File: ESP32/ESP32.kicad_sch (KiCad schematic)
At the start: 0 parts

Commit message: ESP32
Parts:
- added C1: C_Small, symbol Device:C_Small
- added D1: D, symbol Device:D
- added U1: ESP32-S3, Package_DFN_QFN:QFN-56-1EP_7x7mm_P0.4mm_EP4x4mm, symbol MCU_Espressif:ESP32-S3
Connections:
- new net: U1.2 (VDD3P3), U1.3 (VDD3P3)
- new net: U1.55 (VDDA), U1.56 (VDDA)

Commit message: Upload ESP32
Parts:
- added C1, C4, C5: TBD, symbol Device:C_Small
- added C10, C13, C14, C15: 0.1uF, symbol Device:C_Small
- added C2: 1u, symbol Device:C_Small
- added C3: 10n, symbol Device:C_Small
- added L2, L4, L5: 24nH, symbol Device:L
- added R1: 10k(NC), symbol Device:R_US
- added R10, R13, R14, R15, R16: 0, symbol Device:R_US
- added R3: 499, symbol Device:R_US
- added Y1: Crystal, symbol Device:Crystal
- C21: renamed from C1; value C_Small -> 10u
- D1: value D -> ESD
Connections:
- net +3V3: now also C21.1, D1.1 (K), U1.20 (VDD3P3_RTC), U1.46 (VDD3P3_CPU), C10.1, C15.1, C2.1, C3.1, R1.2
- net GNDREF: now also C21.2, D1.2 (A), U1.57 (GND), C1.2, C10.2, C13.2, C14.1, C15.2, C2.2, C4.2, C5.2
- net GPIO5: now reaches U1.10 (GPIO5)
- net GPIO6: now reaches U1.11 (GPIO6)
- net GPIO7: now reaches U1.12 (GPIO7)
- net GPIO8: now reaches U1.13 (GPIO8)
- net GPIO9: now reaches U1.14 (GPIO9)
- net GPIO10: now reaches U1.15 (GPIO10)
- net GPIO11: now reaches U1.16 (GPIO11)
- net GPIO12: now reaches U1.17 (GPIO12)
- net GPIO13: now reaches U1.18 (GPIO13)
- net GPIO14: now reaches U1.19 (GPIO14)
- net GPIO17: now reaches U1.23 (GPIO17)
- net GPIO18: now reaches U1.24 (GPIO18)
- net GPIO19: now reaches U1.25 (GPIO19/USB_D-)
- net GPIO20: now reaches U1.26 (GPIO20/USB_D+)
- net GPIO21: now reaches U1.27 (GPIO21)
- net GPIO26: now reaches U1.28 (SPICS1)
- net VDD_SPI: now reaches U1.29 (VDD_SPI)
- net VDD_SPI: now also C13.1, C14.2
- net at U1.30 (SPIHD): now also R13.2
- net at U1.31 (SPIWP): now also R14.2
- net SPIS0: now reaches U1.32 (SPICS0)
- net at U1.33 (SPICLK): now also R10.2
- net at U1.34 (SPIQ): now also R15.2
- net at U1.35 (SPID): now also R16.2
- net GPIO48: now reaches U1.36 (SPICLK_N)
- net GPIO47: now reaches U1.37 (SPICLK_P)
- net GPIO33: now reaches U1.38 (GPIO33)
- net GPIO34: now reaches U1.39 (GPIO34)
- net CHIP_PU: now reaches U1.4 (CHIP_PU)
- net GPIO35: now reaches U1.40 (GPIO35)
- net GPIO36: now reaches U1.41 (GPIO36)
- net GPIO37: now reaches U1.42 (GPIO37)
- net GPIO38: now reaches U1.43 (GPIO38)
- net GPIO39: now reaches U1.44 (MTCK)
- net GPIO40: now reaches U1.45 (MTDO)
- net GPIO41: now reaches U1.47 (MTDI)
- net GPIO42: now reaches U1.48 (MTMS)
- net at U1.49 (U0TXD): now also R3.2
- net GPIO0: now reaches U1.5 (GPIO0)
- net U0RXD: now reaches U1.50 (U0RXD)
- net GPIO45: now reaches U1.51 (GPIO45)
- net GPIO45: now also R1.1
- net GPIO46: now reaches U1.52 (GPIO46)
- net 40MHz(10ppm): now reaches U1.53 (XTAL_N)
- net 40MHz(10ppm): now also C4.1, L4.1, Y1.2
- net at U1.54 (XTAL_P): now also L4.2
- net at U1.55 (VDDA), U1.56 (VDDA): now also C3.2
- net GPIO1: now reaches U1.6 (GPIO1)
- net GPIO2: now reaches U1.7 (GPIO2)
- net GPIO3: now reaches U1.8 (GPIO3)
- net GPIO4: now reaches U1.9 (GPIO4)
- new net: C1.1, Y1.1
- new net LNA_IN: L2.1
- new net SPICLK: R10.1
- new net SPID: R16.1
- new net SPIHD: R13.1
- new net SPIQ: R15.1
- new net SPIWP: R14.1
- new net U0TXD: R3.1
- no-connect marks 0 -> 1
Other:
- title: (none) -> ESP32-S3
- moved on the sheet: C21, D1, U1

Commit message: Upload ESP32
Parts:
- added U2: W25Q128JV, Package_SON:WSON-8-1EP_8x6mm_P1.27mm_EP3.4x4.3mm, symbol Memory_Flash:W25Q128JVE
- added U3: APS1604M-3SQRx-SN, Package_SO:SOIC-8_3.9x4.9mm_P1.27mm, symbol Memory_RAM:APS1604M-3SQRx-SN
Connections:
- net GNDREF: now also U2.4 (GND)
- net SPICLK: now also U2.6 (CLK)
- net SPID: now also U2.2 (DO/IO_{1})
- net SPIHD: now also U2.5 (DI/IO_{0})
- net SPIQ: now also U2.3 (~{WP}/IO_{2})
- net SPIWP: now also U2.7 (~{HOLD}/~{RESET}/IO_{3})
- new net SPICS0: U2.1 (~{CS})
- new net VDD: U2.8 (VCC)

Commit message: Upload ESP32
Version 5
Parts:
- added C6, C7: C_Small, symbol Device:C_Small
- added P1: USB_C_Plug_USB2.0, symbol Connector:USB_C_Plug_USB2.0
- added R13, R14: 22/33, symbol Device:R_US
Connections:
- net GNDREF: now also U3.4 (VSS), C6.1, C7.2
- net GPIO26: now also U3.1 (~{CE})
- net SPICLK: now also U3.6 (SCLK)
- net SPID: now also U3.5 (SI/SIO0)
- net SPIHD: now also U3.7 (SIO3)
- net SPIQ: now also U3.2 (SO/SIO1)
- net SPIWP: now also U3.3 (SIO2)
- net VDD: now also U3.8 (VDD)
- new net: C7.1, P1.A6 (D+), R14.1
- new net: P1.A1 (GND), P1.A12 (GND), P1.B1 (GND), P1.B12 (GND)
- new net: P1.A4 (VBUS), P1.A9 (VBUS), P1.B4 (VBUS), P1.B9 (VBUS)
- new net: C6.2, P1.A7 (D-), R13.1
- new net USB_DM: R14.2
- new net USB_DP: R13.2
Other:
- added sheet Wi-Fi Module (Wi-Fi Module_sch.kicad_sch)
- note added: "FLASH-3V3"
- note added: "PSRAM-3V3"
- moved on the sheet: U3

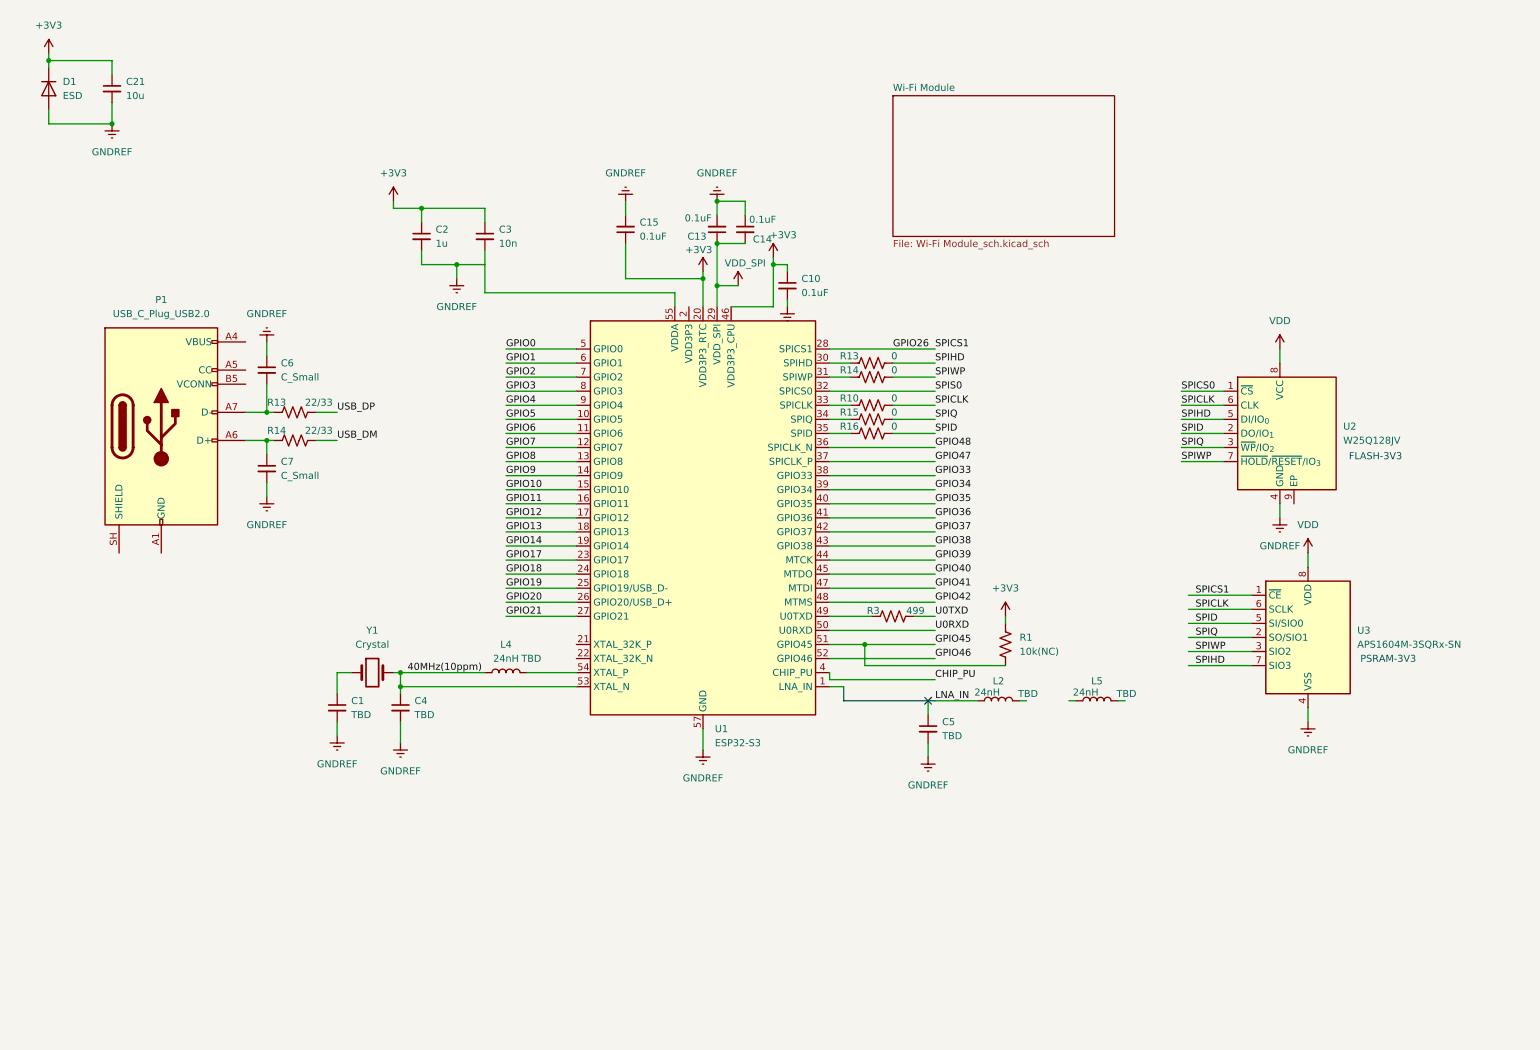
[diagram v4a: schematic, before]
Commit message: Upload ESP32
Version 6
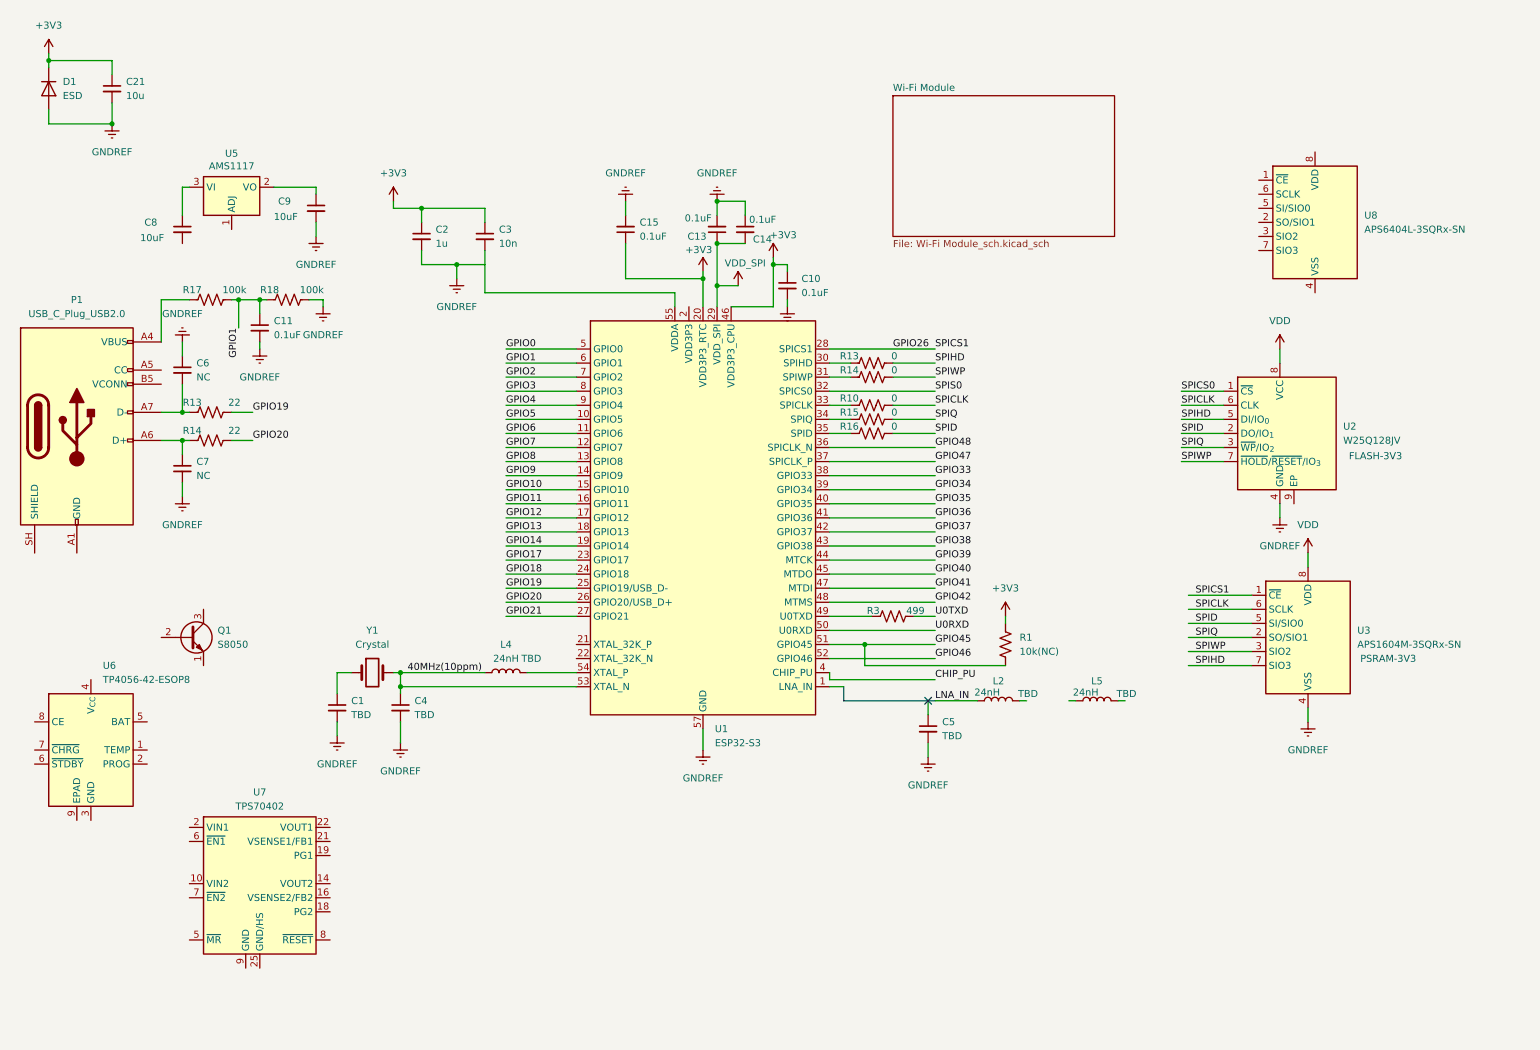
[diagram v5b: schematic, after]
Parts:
- added C11: 0.1uF, symbol Device:C_Small
- added C8, C9: 10uF, symbol Device:C_Small
- added Q1: S8050, Package_TO_SOT_THT:TO-92_Inline, symbol Transistor_BJT:S8050
- added R17, R18: 100k, symbol Device:R_US
- added U5: AMS1117, Package_TO_SOT_SMD:SOT-223-3_TabPin2, symbol Regulator_Linear:AMS1117
- added U6: TP4056-42-ESOP8, Package_SO:SOIC-8-1EP_3.9x4.9mm_P1.27mm_EP2.41x3.3mm_ThermalVias, symbol Battery_Management:TP4056-42-ESOP8
- added U7: TPS70402, Package_SO:HTSSOP-24-1EP_4.4x7.8mm_P0.65mm_EP3.4x7.8mm_Mask2.4x4.68mm_ThermalVias, symbol Regulator_Linear:TPS70402
- added U8: APS6404L-3SQRx-SN, Package_SO:SOIC-8_3.9x4.9mm_P1.27mm, symbol Memory_RAM:APS6404L-3SQRx-SN
- C6, C7: value C_Small -> NC
- R13, R14: value 22/33 -> 22
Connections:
- net USB_DM is gone; now on net GPIO20: R14.2
- net USB_DP is gone; now on net GPIO19: R13.2
- net GNDREF: now also C11.2, C9.2, R18.2
- net GPIO1: now also C11.1, R17.2, R18.1
- net at P1.A4 (VBUS), P1.A9 (VBUS), P1.B4 (VBUS)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: now also R17.1
- new net: C9.1, U5.2 (VO)
- new net: C8.1, U5.3 (VI)
- new net: U7.1 (GND/HS), U7.12 (GND/HS), U7.13 (GND/HS), U7.24 (GND/HS), U7.25 (GND/HS)
- new net: U7.10 (VIN2), U7.11 (VIN2)
- new net: U7.14 (VOUT2), U7.15 (VOUT2)
- new net: U7.2 (VIN1), U7.3 (VIN1)
- new net: U7.22 (VOUT1), U7.23 (VOUT1)
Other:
- moved on the sheet: C6, C7, P1, R13, R14

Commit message: Upload ESP32
Version 8
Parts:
- removed U8: APS6404L-3SQRx-SN, Package_SO:SOIC-8_3.9x4.9mm_P1.27mm, symbol Memory_RAM:APS6404L-3SQRx-SN
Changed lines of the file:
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@@
-	)
-	(symbol
-		(lib_id "Memory_RAM:APS6404L-3SQRx-SN")
-		(at 247.65 49.53 0)
-		(unit 1)
-		(body_style 1)
-		(exclude_from_sim no)
-		(in_bom yes)
-		(on_board yes)
-		(in_pos_files yes)
-		(dnp no)
-		(fields_autoplaced yes)
-		(property "Reference" "U8"
-			(at 256.54 48.2599 0)
-			(show_name no)
-			(do_not_autoplace no)
-			(effects
-				(font
-					(size 1.27 1.27)
-				)
-				(justify left)
-			)
-		)
-		(property "Value" "APS6404L-3SQRx-SN"
-			(at 256.54 50.7999 0)
-			(show_name no)
-			(do_not_autoplace no)
-			(effects
-				(font
-					(size 1.27 1.27)
-				)
-				(justify left)
-			)
-		)
-		(property "Footprint" "Package_SO:SOIC-8_3.9x4.9mm_P1.27mm"
-			(at 247.65 64.77 0)
-			(hide yes)
-			(show_name no)
-			(do_not_autoplace no)
-			(effects
-				(font
-					(size 1.27 1.27)
-				)
-			)
-		)
-		(property "Datasheet" "https://www.mouser.com/datasheet/2/1127/APM_PSRAM_QSPI_APS6404L_3SQR_v2_3_PKG-1954826.pdf"
-			(at 247.65 67.31 0)
-			(hide yes)
-			(show_name no)
-			(do_not_autoplace no)
-			(effects
-				(font
-					(size 1.27 1.27)
-				)
-			)
-		)
-		(property "Description" "64 Mbit / 8M x 8-bits serial pseudo SRAM MEMORY, up to 133MHz, 2.7-3.6V supply, SOIC-8 (SOP-8)"
-			(at 247.65 69.85 0)
-			(hide yes)
-			(show_name no)
-			(do_not_autoplace no)
-			(effects
-				(font
-					(size 1.27 1.27)
-				)
-			)
-		)
-		(pin "6"
-		)
-		(pin "2"
-		)
-		(pin "5"
-		)
-		(pin "8"
-		)
-		(pin "7"
-		)
-		(pin "1"
-		)
-		(pin "3"
-		)
-		(pin "4"
-		)
-		(instances
-			(project "ESP32"
-				(path "/21854826-38d8-4bae-b9c0-6b760ec4509b"
-					(reference "U8")
-					(unit 1)
-				)
-			)
-		)
 	)
 	(symbol
